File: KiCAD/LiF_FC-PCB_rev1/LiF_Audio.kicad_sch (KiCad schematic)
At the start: 21 parts, among them J28 Amp V select, J29 ST 1 Bypass, J30 ST 2 Bypass, J31 Vol Pot Bypass, J32 SKP OUT, U12 PAM8302AAS

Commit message: fixing ERC bugs on schematic. Only MCU left
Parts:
- added TP3: Audio_{OUT}, TestPoint:TestPoint_Bridge_Pitch2.54mm_Drill1.0mm, symbol Connector:TestPoint
- added TP4: Audio_{REF}, TestPoint:TestPoint_Bridge_Pitch2.54mm_Drill1.0mm, symbol Connector:TestPoint
- added TP5: Audio_{IN}, TestPoint:TestPoint_Bridge_Pitch2.54mm_Drill1.0mm, symbol Connector:TestPoint
- RV1: value R_Potentiometer -> 10k; footprint (none) -> Potentiometer_SMD:Potentiometer_Bourns_TC33X_Vertical; DKPN (none) -> TC33X-103ECT-ND; PN (none) -> TC33X-2-103E
- TP1: DKPN (none) -> 36-5002-ND; PN (none) -> 5002
- TP2: footprint TestPoint:TestPoint_Bridge_Pitch2.54mm_Drill1.0mm -> TestPoint:TestPoint_Loop_D1.80mm_Drill1.0mm_Beaded; DKPN (none) -> 36-5002-ND; PN (none) -> 5002
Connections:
- net at C06_3.2, U12.3 (IN+): now also TP5.1
- net at J32.1 (Pin_1), LS1.1, U12.5 (OUT+): now also TP3.1
- net at J32.2 (Pin_2), LS1.2, U12.8 (OUT-): now also TP4.1

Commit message: Added MCU pinout, shanged shift registers to GPIO expanders to save pins on MCU
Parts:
- renumbered J28 to J29, J29 to J30, J30 to J31, J31 to J32, J32 to J33, R54 to R55, R55 to R56, TP3 to TP22, TP4 to TP23, TP1 to TP24, TP2 to TP25, TP5 to TP26
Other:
- title: (none) -> Lithium Firefly Custom FC/CC PCB

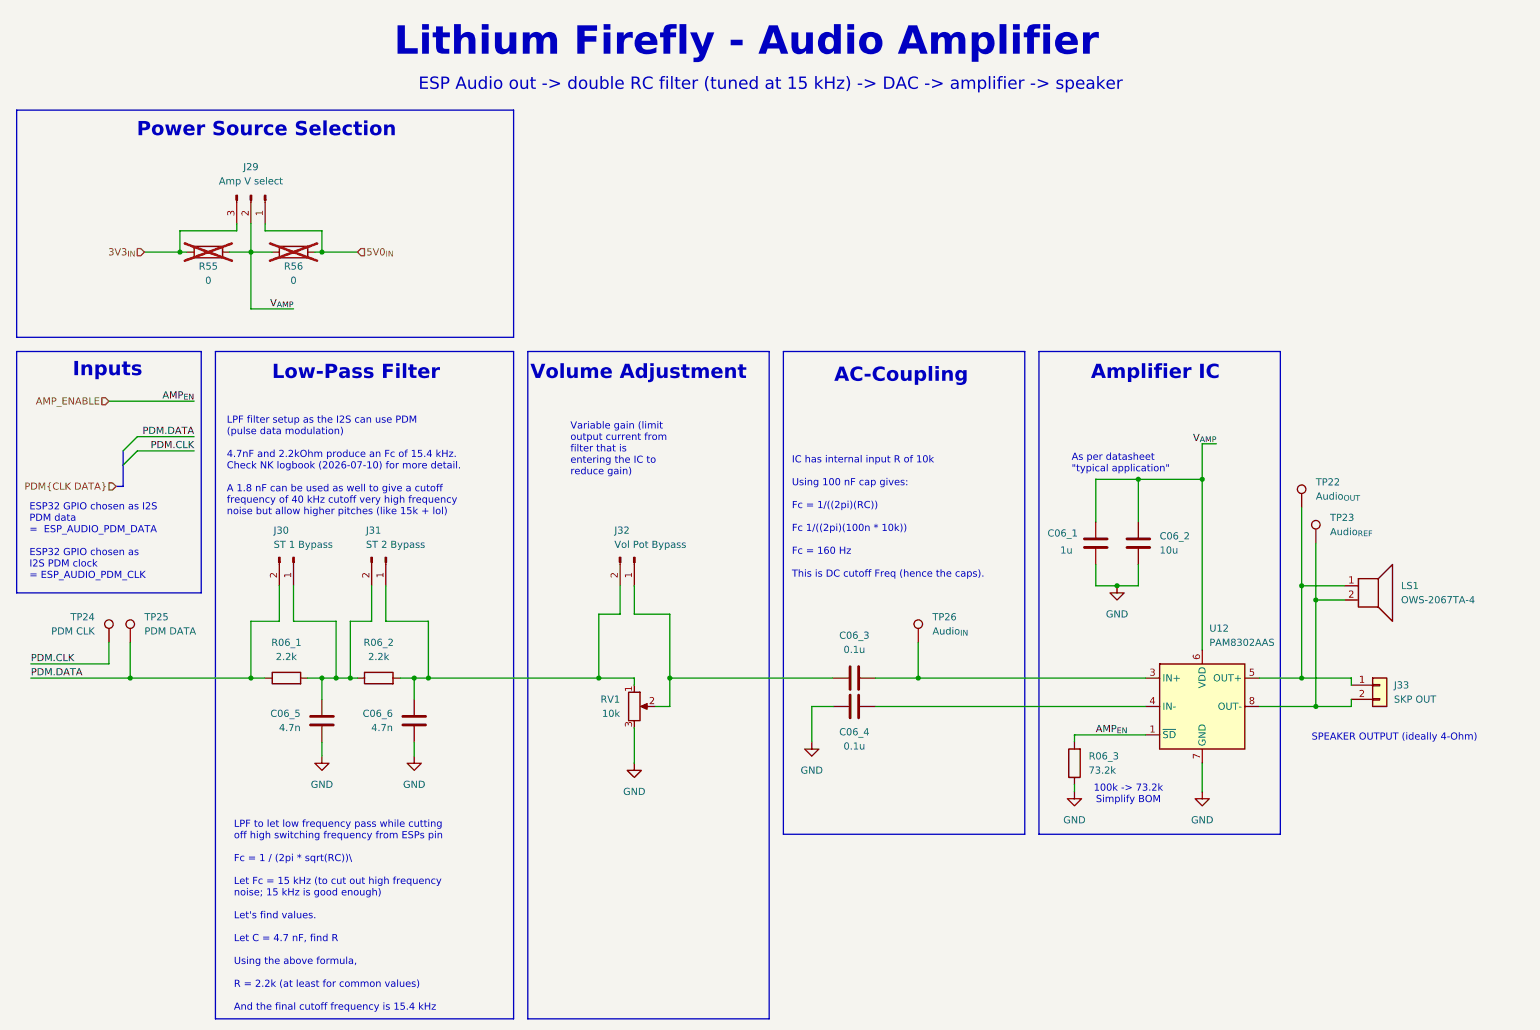
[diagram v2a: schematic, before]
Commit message: Finalized schematic diagram. Only needs formatting fixes and resistor component sourcing info
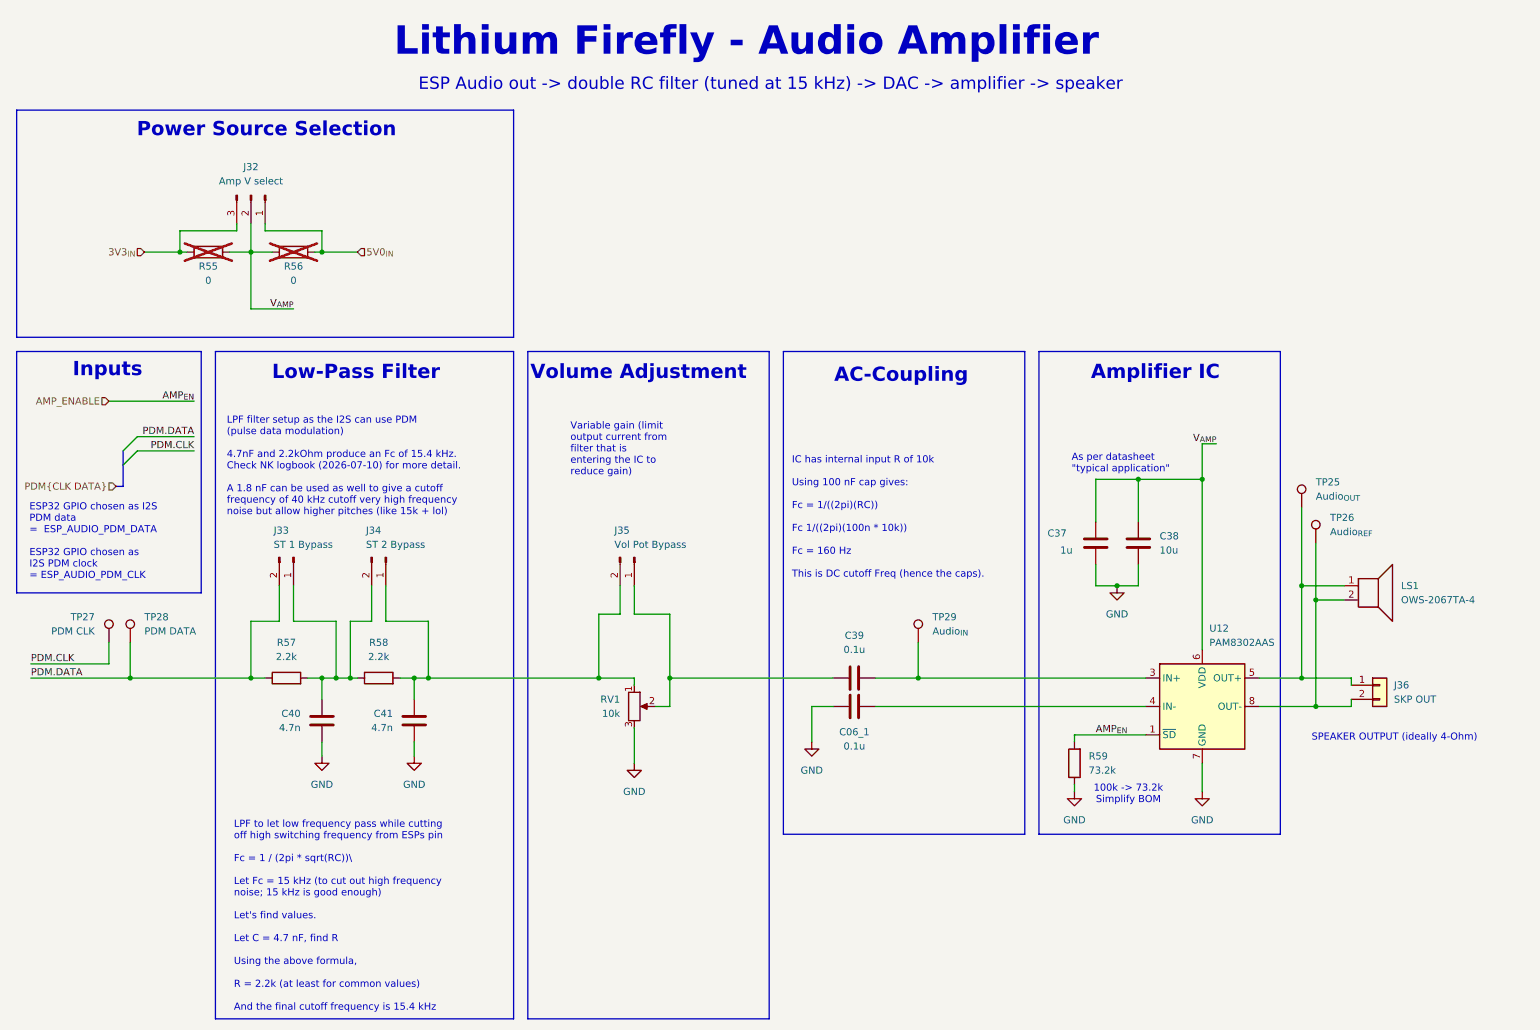
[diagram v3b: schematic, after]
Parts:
- renumbered C06_4 to C06_1, C06_1 to C37, C06_2 to C38, C06_3 to C39, C06_5 to C40, C06_6 to C41, J29 to J32, J30 to J33, J31 to J34, J32 to J35, J33 to J36, R06_1 to R57, R06_2 to R58, R06_3 to R59, TP22 to TP25, TP23 to TP26, TP24 to TP27, TP25 to TP28, TP26 to TP29
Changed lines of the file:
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@@
 		(dnp no)
 		(fields_autoplaced yes)
-		(property "Reference" "#PWR078"
+		(property "Reference" "#PWR081"
 			(at 228.6 158.75 0)
 			(effects
@@
 			(project "LiF_FC-PCB_rev1"
 				(path "/9e3e8da7-e506-46c9-90e5-307e4ad30d29/75541181-887f-448c-8628-82c2df7284ca"
-					(reference "#PWR078")
+					(reference "#PWR081")
 					(unit 1)
 				)
@@
 		(on_board yes)
 		(dnp no)
-		(property "Reference" "C06_2"
+		(property "Reference" "C38"
 			(at 220.98 106.6799 0)
 			(effects
@@
 			(project "LiF_FC-PCB_rev1"
 				(path "/9e3e8da7-e506-46c9-90e5-307e4ad30d29/75541181-887f-448c-8628-82c2df7284ca"
-					(reference "C06_2")
+					(reference "C38")
 					(unit 1)
 				)
@@
 		(on_board yes)
 		(dnp no)
-		(property "Reference" "C06_5"
+		(property "Reference" "C40"
 			(at 67.31 138.4299 0)
 			(effects
@@
 			(project "LiF_FC-PCB_rev1"
 				(path "/9e3e8da7-e506-46c9-90e5-307e4ad30d29/75541181-887f-448c-8628-82c2df7284ca"
-					(reference "C06_5")
+					(reference "C40")
 					(unit 1)
 				)
@@
 		(dnp no)
 		(fields_autoplaced yes)
-		(property "Reference" "C06_3"
+		(property "Reference" "C39"
 			(at 166.37 124.46 90)
 			(effects
@@
 			(project "LiF_FC-PCB_rev1"
 				(path "/9e3e8da7-e506-46c9-90e5-307e4ad30d29/75541181-887f-448c-8628-82c2df7284ca"
-					(reference "C06_3")
+					(reference "C39")
 					(unit 1)
 				)
@@
 		(on_board yes)
 		(dnp no)
-		(property "Reference" "J31"
+		(property "Reference" "J34"
 			(at 78.994 105.664 90)
 			(effects
@@
 			(project "LiF_FC-PCB_rev1"
 				(path "/9e3e8da7-e506-46c9-90e5-307e4ad30d29/75541181-887f-448c-8628-82c2df7284ca"
-					(reference "J31")
+					(reference "J34")
 					(unit 1)
 				)
@@
 		(dnp no)
 		(fields_autoplaced yes)
-		(property "Reference" "#PWR075"
+		(property "Reference" "#PWR078"
 			(at 87.63 152.4 0)
 			(effects
@@
 			(project "LiF_FC-PCB_rev1"
 				(path "/9e3e8da7-e506-46c9-90e5-307e4ad30d29/75541181-887f-448c-8628-82c2df7284ca"
-					(reference "#PWR075")
+					(reference "#PWR078")
 					(unit 1)
 				)
@@
 		(dnp no)
 		(fields_autoplaced yes)
-		(property "Reference" "R06_1"
+		(property "Reference" "R57"
 			(at 64.77 125.73 90)
 			(effects
@@
 			(project "LiF_FC-PCB_rev1"
 				(path "/9e3e8da7-e506-46c9-90e5-307e4ad30d29/75541181-887f-448c-8628-82c2df7284ca"
-					(reference "R06_1")
+					(reference "R57")
 					(unit 1)
 				)
@@
 		(on_board yes)
 		(dnp no)
-		(property "Reference" "J30"
+		(property "Reference" "J33"
 			(at 62.484 105.664 90)
 			(effects
@@
 			(project "LiF_FC-PCB_rev1"
 				(path "/9e3e8da7-e506-46c9-90e5-307e4ad30d29/75541181-887f-448c-8628-82c2df7284ca"
-					(reference "J30")
+					(reference "J33")
 					(unit 1)
 				)
@@
 		(dnp no)
 		(fields_autoplaced yes)
-		(property "Reference" "J29"
+		(property "Reference" "J32"
 			(at 58.42 40.64 90)
 			(effects
@@
 			(project "LiF_FC-PCB_rev1"
 				(path "/9e3e8da7-e506-46c9-90e5-307e4ad30d29/75541181-887f-448c-8628-82c2df7284ca"
-					(reference "J29")
+					(reference "J32")
 					(unit 1)
 				)
@@
 		(on_board yes)
 		(dnp no)
-		(property "Reference" "TP22"
+		(property "Reference" "TP25"
 			(at 248.92 97.0279 0)
 			(effects
@@
 			(project "LiF_FC-PCB_rev1"
 				(path "/9e3e8da7-e506-46c9-90e5-307e4ad30d29/75541181-887f-448c-8628-82c2df7284ca"
-					(reference "TP22")
+					(reference "TP25")
 					(unit 1)
 				)
@@
 		(on_board yes)
 		(dnp no)
-		(property "Reference" "TP26"
+		(property "Reference" "TP29"
 			(at 180.34 121.1579 0)
 			(effects
@@
 			(project "LiF_FC-PCB_rev1"
 				(path "/9e3e8da7-e506-46c9-90e5-307e4ad30d29/75541181-887f-448c-8628-82c2df7284ca"
-					(reference "TP26")
+					(reference "TP29")
 					(unit 1)
 				)
@@
 		(on_board yes)
 		(dnp no)
-		(property "Reference" "C06_1"
+		(property "Reference" "C37"
 			(at 200.914 106.172 0)
 			(effects
@@
 			(project "LiF_FC-PCB_rev1"
 				(path "/9e3e8da7-e506-46c9-90e5-307e4ad30d29/75541181-887f-448c-8628-82c2df7284ca"
-					(reference "C06_1")
+					(reference "C37")
 					(unit 1)
 				)
@@
 		(dnp no)
 		(fields_autoplaced yes)
-		(property "Reference" "R06_2"
+		(property "Reference" "R58"
 			(at 81.28 125.73 90)
 			(effects
@@
 			(project "LiF_FC-PCB_rev1"
 				(path "/9e3e8da7-e506-46c9-90e5-307e4ad30d29/75541181-887f-448c-8628-82c2df7284ca"
-					(reference "R06_2")
+					(reference "R58")
 					(unit 1)
 				)
@@
 		(on_board yes)
 		(dnp no)
-		(property "Reference" "TP23"
+		(property "Reference" "TP26"
 			(at 251.46 103.3779 0)
 			(effects
@@
 			(project "LiF_FC-PCB_rev1"
 				(path "/9e3e8da7-e506-46c9-90e5-307e4ad30d29/75541181-887f-448c-8628-82c2df7284ca"
-					(reference "TP23")
+					(reference "TP26")
 					(unit 1)
 				)
@@
 		(dnp no)
 		(fields_autoplaced yes)
-		(property "Reference" "J33"
+		(property "Reference" "J36"
 			(at 262.89 133.3499 0)
 			(effects
@@
 			(project "LiF_FC-PCB_rev1"
 				(path "/9e3e8da7-e506-46c9-90e5-307e4ad30d29/75541181-887f-448c-8628-82c2df7284ca"
-					(reference "J33")
+					(reference "J36")
 					(unit 1)
 				)
@@
 		(on_board yes)
 		(dnp no)
-		(property "Reference" "C06_4"
+		(property "Reference" "C06_1"
 			(at 166.37 141.732 90)
 			(effects
@@
 			(project "LiF_FC-PCB_rev1"
 				(path "/9e3e8da7-e506-46c9-90e5-307e4ad30d29/75541181-887f-448c-8628-82c2df7284ca"
-					(reference "C06_4")
+					(reference "C06_1")
 					(unit 1)
 				)
@@
 		(dnp no)
 		(fields_autoplaced yes)
-		(property "Reference" "#PWR076"
+		(property "Reference" "#PWR079"
 			(at 127 153.67 0)
 			(effects
@@
 			(project "LiF_FC-PCB_rev1"
 				(path "/9e3e8da7-e506-46c9-90e5-307e4ad30d29/75541181-887f-448c-8628-82c2df7284ca"
-					(reference "#PWR076")
+					(reference "#PWR079")
 					(unit 1)
 				)
@@
 		(dnp no)
 		(fields_autoplaced yes)
-		(property "Reference" "#PWR072"
+		(property "Reference" "#PWR075"
 			(at 213.36 121.92 0)
 			(effects
@@
 			(project "LiF_FC-PCB_rev1"
 				(path "/9e3e8da7-e506-46c9-90e5-307e4ad30d29/75541181-887f-448c-8628-82c2df7284ca"
-					(reference "#PWR072")
+					(reference "#PWR075")
 					(unit 1)
 				)
@@
 		(on_board yes)
 		(dnp no)
-		(property "Reference" "TP24"
+		(property "Reference" "TP27"
 			(at 30.48 121.1579 0)
 			(effects
@@
 			(project "LiF_FC-PCB_rev1"
 				(path "/9e3e8da7-e506-46c9-90e5-307e4ad30d29/75541181-887f-448c-8628-82c2df7284ca"
-					(reference "TP24")
+					(reference "TP27")
 					(unit 1)
 				)
@@
 		(dnp no)
 		(fields_autoplaced yes)
-		(property "Reference" "#PWR074"
+		(property "Reference" "#PWR077"
 			(at 71.12 152.4 0)
 			(effects
@@
 			(project "LiF_FC-PCB_rev1"
 				(path "/9e3e8da7-e506-46c9-90e5-307e4ad30d29/75541181-887f-448c-8628-82c2df7284ca"
-					(reference "#PWR074")
+					(reference "#PWR077")
 					(unit 1)
 				)
@@
 		(dnp no)
 		(fields_autoplaced yes)
-		(property "Reference" "#PWR077"
+		(property "Reference" "#PWR080"
 			(at 205.74 158.75 0)
 			(effects
@@
 			(project "LiF_FC-PCB_rev1"
 				(path "/9e3e8da7-e506-46c9-90e5-307e4ad30d29/75541181-887f-448c-8628-82c2df7284ca"
-					(reference "#PWR077")
+					(reference "#PWR080")
 					(unit 1)
 				)
@@
 		(dnp no)
 		(fields_autoplaced yes)
-		(property "Reference" "#PWR073"
+		(property "Reference" "#PWR076"
 			(at 158.75 149.86 0)
 			(effects
@@
 			(project "LiF_FC-PCB_rev1"
 				(path "/9e3e8da7-e506-46c9-90e5-307e4ad30d29/75541181-887f-448c-8628-82c2df7284ca"
-					(reference "#PWR073")
+					(reference "#PWR076")
 					(unit 1)
 				)
@@
 		(dnp no)
 		(fields_autoplaced yes)
-		(property "Reference" "TP25"
+		(property "Reference" "TP28"
 			(at 39.37 121.1579 0)
 			(effects
@@
 			(project "LiF_FC-PCB_rev1"
 				(path "/9e3e8da7-e506-46c9-90e5-307e4ad30d29/75541181-887f-448c-8628-82c2df7284ca"
-					(reference "TP25")
+					(reference "TP28")
 					(unit 1)
 				)
@@
 		(on_board yes)
 		(dnp no)
-		(property "Reference" "C06_6"
+		(property "Reference" "C41"
 			(at 83.82 138.4299 0)
 			(effects
@@
 			(project "LiF_FC-PCB_rev1"
 				(path "/9e3e8da7-e506-46c9-90e5-307e4ad30d29/75541181-887f-448c-8628-82c2df7284ca"
-					(reference "C06_6")
+					(reference "C41")
 					(unit 1)
 				)
@@
 		(on_board yes)
 		(dnp no)
-		(property "Reference" "J32"
+		(property "Reference" "J35"
 			(at 123.444 105.664 90)
 			(effects
@@
 			(project "LiF_FC-PCB_rev1"
 				(path "/9e3e8da7-e506-46c9-90e5-307e4ad30d29/75541181-887f-448c-8628-82c2df7284ca"
-					(reference "J32")
+					(reference "J35")
 					(unit 1)
 				)
@@
 		(dnp no)
 		(fields_autoplaced yes)
-		(property "Reference" "R06_3"
+		(property "Reference" "R59"
 			(at 208.28 146.0499 0)
 			(effects
@@
 			(project "LiF_FC-PCB_rev1"
 				(path "/9e3e8da7-e506-46c9-90e5-307e4ad30d29/75541181-887f-448c-8628-82c2df7284ca"
-					(reference "R06_3")
-					(unit 1)
-				)
+					(reference "R59")
+					(unit 1)
+				)

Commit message: set up board configuration and started routing PCB
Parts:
- TP25, TP26, TP27, TP29: footprint TestPoint:TestPoint_Bridge_Pitch2.54mm_Drill1.0mm -> TestPoint:TestPoint_Loop_D1.80mm_Drill1.0mm_Beaded
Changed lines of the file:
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@@
 			)
 		)
-		(property "Footprint" "TestPoint:TestPoint_Bridge_Pitch2.54mm_Drill1.0mm"
+		(property "Footprint" "TestPoint:TestPoint_Loop_D1.80mm_Drill1.0mm_Beaded"
 			(at 251.46 101.6 0)
 			(effects
@@
 			)
 		)
-		(property "Footprint" "TestPoint:TestPoint_Bridge_Pitch2.54mm_Drill1.0mm"
+		(property "Footprint" "TestPoint:TestPoint_Loop_D1.80mm_Drill1.0mm_Beaded"
 			(at 182.88 125.73 0)
 			(effects
@@
 			)
 		)
-		(property "Footprint" "TestPoint:TestPoint_Bridge_Pitch2.54mm_Drill1.0mm"
+		(property "Footprint" "TestPoint:TestPoint_Loop_D1.80mm_Drill1.0mm_Beaded"
 			(at 254 107.95 0)
 			(effects
@@
 			)
 		)
-		(property "Footprint" "TestPoint:TestPoint_Bridge_Pitch2.54mm_Drill1.0mm"
+		(property "Footprint" "TestPoint:TestPoint_Loop_D1.80mm_Drill1.0mm_Beaded"
 			(at 27.94 125.73 0)
 			(effects

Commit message: backup before leaving school
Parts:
- J32: footprint Connector_PinHeader_2.54mm:PinHeader_1x03_P2.54mm_Vertical -> Connector_PinHeader_2.54mm:PinHeader_1x03_P2.54mm_Vertical_SMD_Pin1Left
- J33, J34, J35: footprint Connector_PinHeader_2.54mm:PinHeader_1x02_P2.54mm_Vertical -> Connector_PinHeader_2.54mm:PinHeader_1x02_P2.54mm_Vertical_SMD_Pin1Left
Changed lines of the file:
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@@
 			)
 		)
-		(property "Footprint" "Connector_PinHeader_2.54mm:PinHeader_1x02_P2.54mm_Vertical"
+		(property "Footprint" "Connector_PinHeader_2.54mm:PinHeader_1x02_P2.54mm_Vertical_SMD_Pin1Left"
 			(at 82.55 110.49 0)
 			(effects
@@
 			)
 		)
-		(property "Footprint" "Connector_PinHeader_2.54mm:PinHeader_1x02_P2.54mm_Vertical"
+		(property "Footprint" "Connector_PinHeader_2.54mm:PinHeader_1x02_P2.54mm_Vertical_SMD_Pin1Left"
 			(at 66.04 110.49 0)
 			(effects
@@
 			)
 		)
-		(property "Footprint" "Connector_PinHeader_2.54mm:PinHeader_1x03_P2.54mm_Vertical"
+		(property "Footprint" "Connector_PinHeader_2.54mm:PinHeader_1x03_P2.54mm_Vertical_SMD_Pin1Left"
 			(at 58.42 45.72 0)
 			(effects
@@
 			)
 		)
-		(property "Footprint" "Connector_PinHeader_2.54mm:PinHeader_1x02_P2.54mm_Vertical"
+		(property "Footprint" "Connector_PinHeader_2.54mm:PinHeader_1x02_P2.54mm_Vertical_SMD_Pin1Left"
 			(at 127 110.49 0)
 			(effects

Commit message: backup before splitting the schematics into 2 boards: I/O PCB and Service PCB
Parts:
- renumbered C06_1 to C58
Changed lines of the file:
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@@
 		(on_board yes)
 		(dnp no)
-		(property "Reference" "C06_1"
+		(property "Reference" "C58"
 			(at 166.37 141.732 90)
 			(effects
@@
 			(project "LiF_FC-PCB_rev1"
 				(path "/9e3e8da7-e506-46c9-90e5-307e4ad30d29/75541181-887f-448c-8628-82c2df7284ca"
-					(reference "C06_1")
+					(reference "C58")
 					(unit 1)
 				)

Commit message: Created new KiCAD project for IO PCB, moved relevant components there, saving backup before reannotating the Service PCB schematics
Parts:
- J32, J33, J34, J35: now not fitted; now left out of the parts list
